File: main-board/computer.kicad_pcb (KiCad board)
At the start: 2 copper layers, 104.1 x 67.3 mm, 17 parts, among them J1 Expansion, J2 Expansion, SW1 RESET, U1 W65C02SxP, U2 28C256, U3 AS6C62256, U4 74HC00, U5 DS1813, X1 1MHz

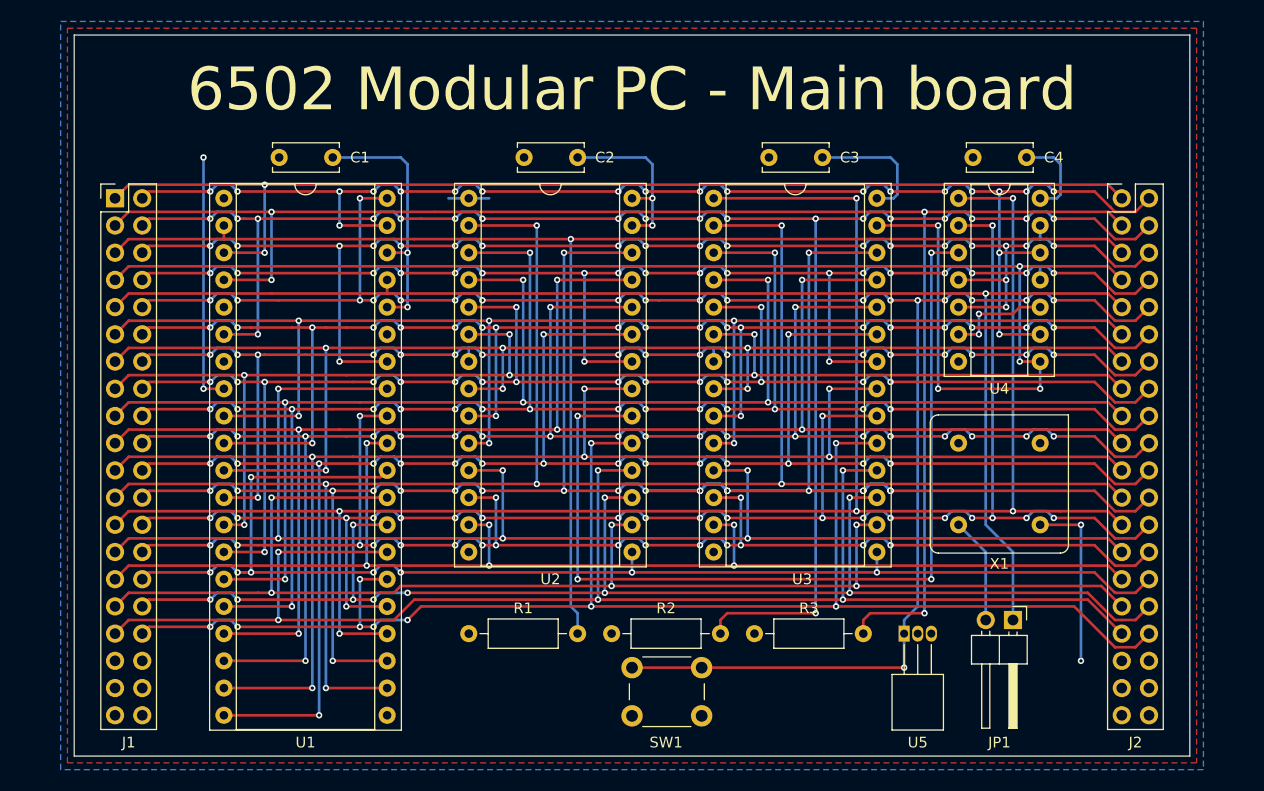
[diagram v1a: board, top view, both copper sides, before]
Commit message: remove vga board, finish other boards
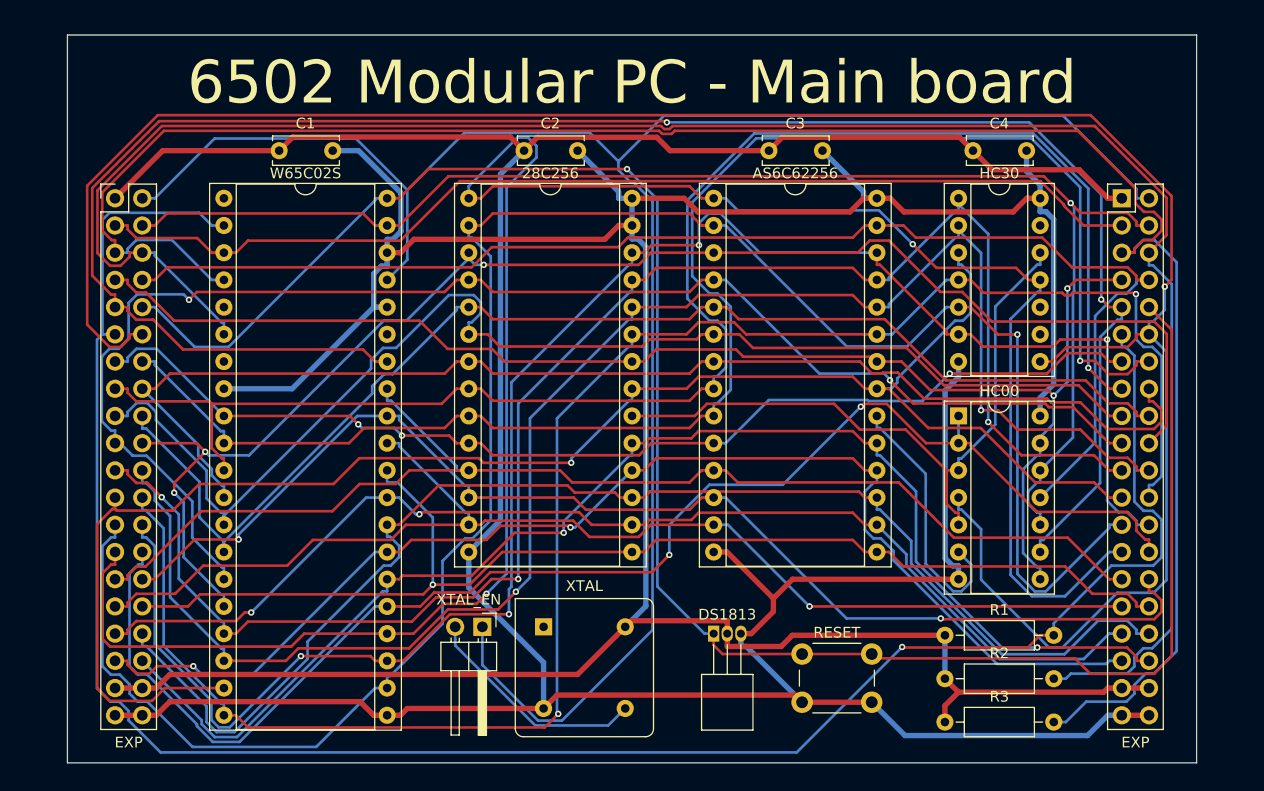
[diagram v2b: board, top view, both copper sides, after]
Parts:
- removed J2: Expansion, Connector_PinHeader_2.54mm:PinHeader_2x20_P2.54mm_Vertical
- removed JP1: Jumper, Connector_PinHeader_2.54mm:PinHeader_1x02_P2.54mm_Horizontal
- removed SW1: RESET, Button_Switch_THT:SW_PUSH_6mm
- removed U1: W65C02SxP, Package_DIP:DIP-40_W15.24mm_Socket
- removed U2: 28C256, Package_DIP:DIP-28_W15.24mm_Socket
- removed U3: AS6C62256, Package_DIP:DIP-28_W15.24mm_Socket
- removed U4: 74HC00, Package_DIP:DIP-14_W7.62mm_Socket
- removed U5: DS1813, Package_TO_SOT_THT:TO-92_Inline_Horizontal1
- removed X1: 1MHz, Oscillator:Oscillator_DIP-8
- added 28C256: 28C256, Package_DIP:DIP-28_W15.24mm_Socket, F.Cu at (104.1, 34.3)
- added AS6C62256: AS6C62256, Package_DIP:DIP-28_W15.24mm_Socket, F.Cu at (127.0, 34.3)
- added DS1813: DS1813, Package_TO_SOT_THT:TO-92_Inline_Horizontal1, F.Cu at (127.0, 74.9)
- added EXP: Expansion, Connector_PinHeader_2.54mm:PinHeader_2x20_P2.54mm_Vertical, F.Cu at (165.1, 34.3)
- added HC00: 74HC00, Package_DIP:DIP-14_W7.62mm_Socket, F.Cu at (149.9, 54.6)
- added HC30: 74HC30, Package_DIP:DIP-14_W7.62mm_Socket, F.Cu at (149.9, 34.3)
- added RESET: RESET, Button_Switch_THT:SW_PUSH_6mm, F.Cu at (135.3, 76.8)
- added W65C02S: W65C02SxP, Package_DIP:DIP-40_W15.24mm_Socket, F.Cu at (81.3, 34.3)
- added XTAL: 1MHz, Oscillator:Oscillator_DIP-8, F.Cu at (111.1, 74.3)
- added XTAL_EN: Jumper, Connector_PinHeader_2.54mm:PinHeader_1x02_P2.54mm_Horizontal, F.Cu at (105.4, 74.3)
- moved R1 44.5 mm to (148.6, 75.1)
- moved R2 31.4 mm to (148.6, 79.1)
- moved R3 19.6 mm to (148.6, 83.2)
- moved C1 0.64 mm to (91.4, 29.8)
- moved C2 0.64 mm to (114.3, 29.8)
- moved C3 0.64 mm to (137.2, 29.8)
- moved C4 0.64 mm to (156.2, 29.8)
- renumbered J1 to EXP
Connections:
- EXP pad 1: PHI1 -> GND
- EXP pad 11: A0 -> RDY
- EXP pad 12: A1 -> !P_SELECT
- EXP pad 13: A2 -> A0
- EXP pad 14: A3 -> A1
- EXP pad 15: A4 -> A2
- EXP pad 16: A5 -> A3
- EXP pad 17: A6 -> A4
- EXP pad 18: A7 -> A5
- EXP pad 19: A8 -> A6
- EXP pad 2: PHI2 -> CLK
- EXP pad 20: A9 -> A7
- EXP pad 21: A10 -> A8
- EXP pad 22: A11 -> A9
- EXP pad 23: A12 -> A10
- EXP pad 24: A13 -> A11
- EXP pad 25: A14 -> A12
- EXP pad 26: !RAM_SELECT -> A13
- EXP pad 27: D0 -> A14
- EXP pad 28: D1 -> A15
- EXP pad 29: D2 -> D0
- EXP pad 3: !IRQ -> PHI1
- EXP pad 30: D3 -> D1
- EXP pad 31: D4 -> D2
- EXP pad 32: D5 -> D3
- EXP pad 33: D6 -> D4
- EXP pad 34: D7 -> D5
- EXP pad 35: +5V -> D6
- EXP pad 36: +5V -> D7
- EXP pad 37: GND -> +5V
- EXP pad 38: GND -> +5V
- EXP pad 4: !NMI -> PHI2
- EXP pad 5: RDY -> !IRQ
- EXP pad 6: R!W -> !NMI
- EXP pad 7: !WRITE -> !READ
- EXP pad 8: !READ -> !WRITE
- EXP pad 9: CLK -> R!W
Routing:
- net GND: track 3.81 -> 319.9 mm
- net !P_SELECT: track 0.00 -> 207.0 mm, vias 0 -> 1
- net +5V: track 101.6 -> 295.7 mm, vias 8 -> 0
- net A15: track 0.00 -> 133.9 mm, vias 0 -> 2
- net !RAM_SELECT: track 156.9 -> 24.8 mm, vias 22 -> 0
- net CLK: track 127.8 -> 186.5 mm, vias 1 -> 0
- net RDY: track 133.4 -> 190.9 mm
- net R!W: track 130.9 -> 178.0 mm, vias 21 -> 2
- net !IRQ: track 150.5 -> 188.0 mm, vias 4 -> 0
- net A13: track 200.7 -> 166.0 mm, vias 22 -> 4
- net A0: track 137.6 -> 103.1 mm, vias 6 -> 3
- net A7: track 164.1 -> 137.6 mm, vias 18 -> 3
- net D6: track 143.6 -> 117.3 mm, vias 6 -> 2
- net A5: track 141.3 -> 117.4 mm, vias 18 -> 0
- net !ROM_SELECT: track 86.4 -> 63.0 mm, vias 4 -> 0
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- removed copper zone on F.Cu, net +5V
- removed copper zone on B.Cu, net GND
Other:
- board size 104.1 x 67.3 mm -> 105.4 x 67.9 mm
- net class Wide added: clearance 0.2, trace_width 0.5, via_dia 0.6, via_drill 0.3
- board text added: "JLCJLCJLCJLC"

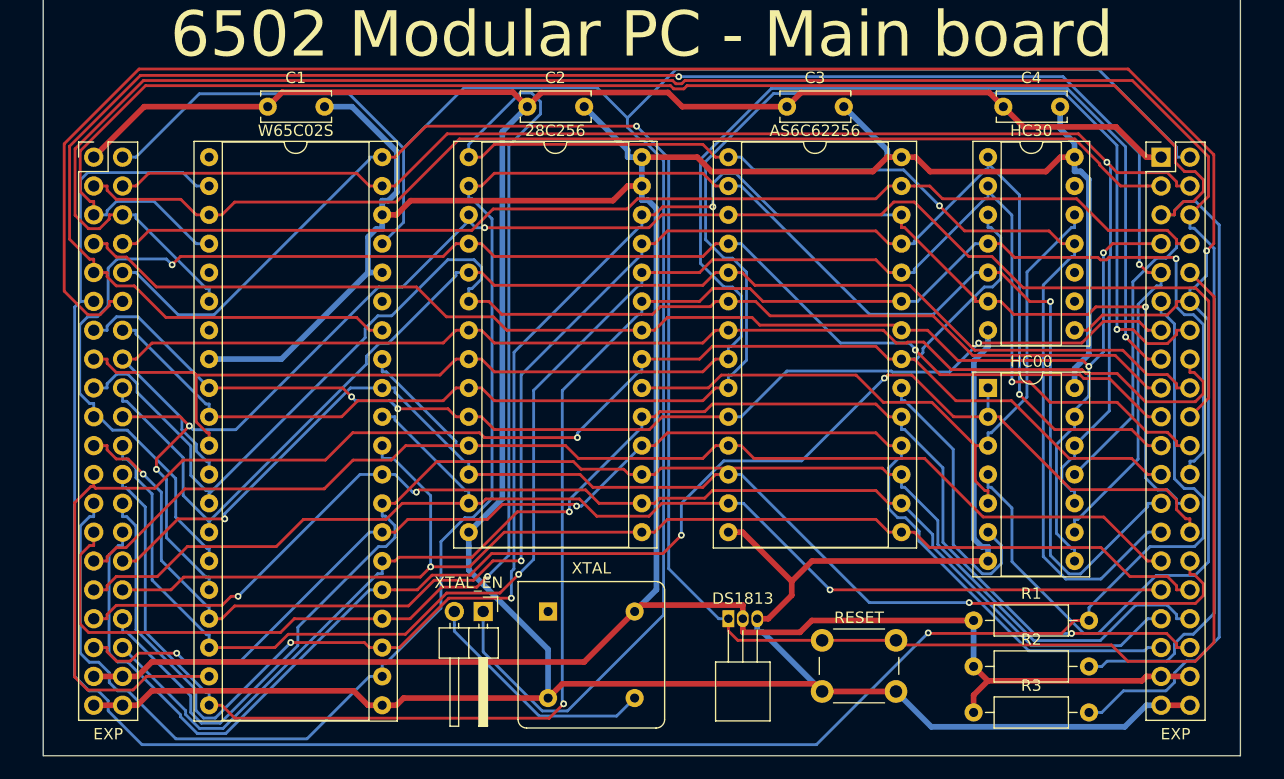
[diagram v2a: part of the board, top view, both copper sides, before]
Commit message: Add VGA socket, fix routing errors on CPU board
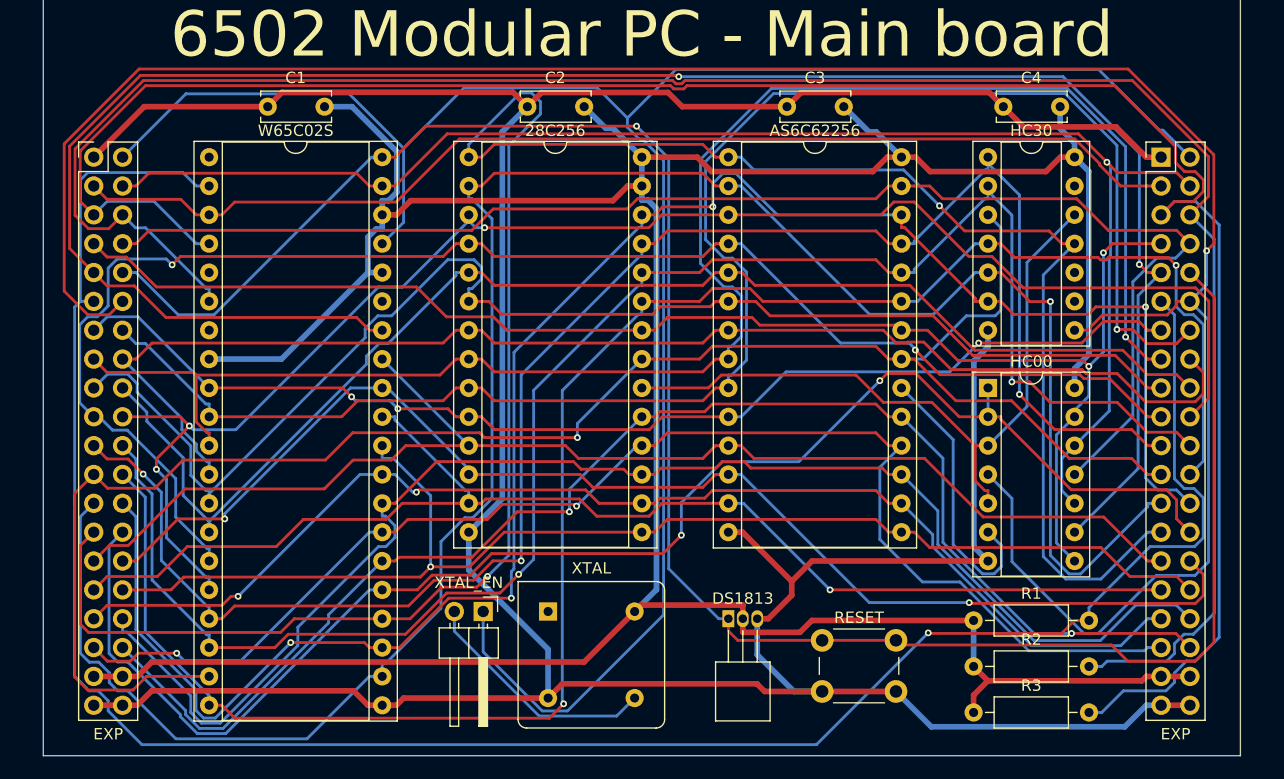
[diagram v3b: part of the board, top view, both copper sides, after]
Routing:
- net D6: track 117.3 -> 119.1 mm
- net A10: track 154.8 -> 156.1 mm
- net D0: track 115.2 -> 114.1 mm
- net +5V: track 295.7 -> 294.7 mm
- net GND: track 319.9 -> 320.7 mm
- net R!W: track 178.0 -> 177.2 mm
- net !IRQ: track 188.0 -> 187.1 mm
- net D1: track 115.5 -> 114.6 mm
- net D7: track 124.5 -> 123.8 mm
- net !NMI: track 183.6 -> 183.0 mm
- net !P_SELECT: track 207.0 -> 206.4 mm
- net A11: track 166.6 -> 166.0 mm
- net PHI2: track 131.7 -> 131.1 mm
- net !READ: track 128.5 -> 127.9 mm
- net CLK: track 186.5 -> 186.0 mm

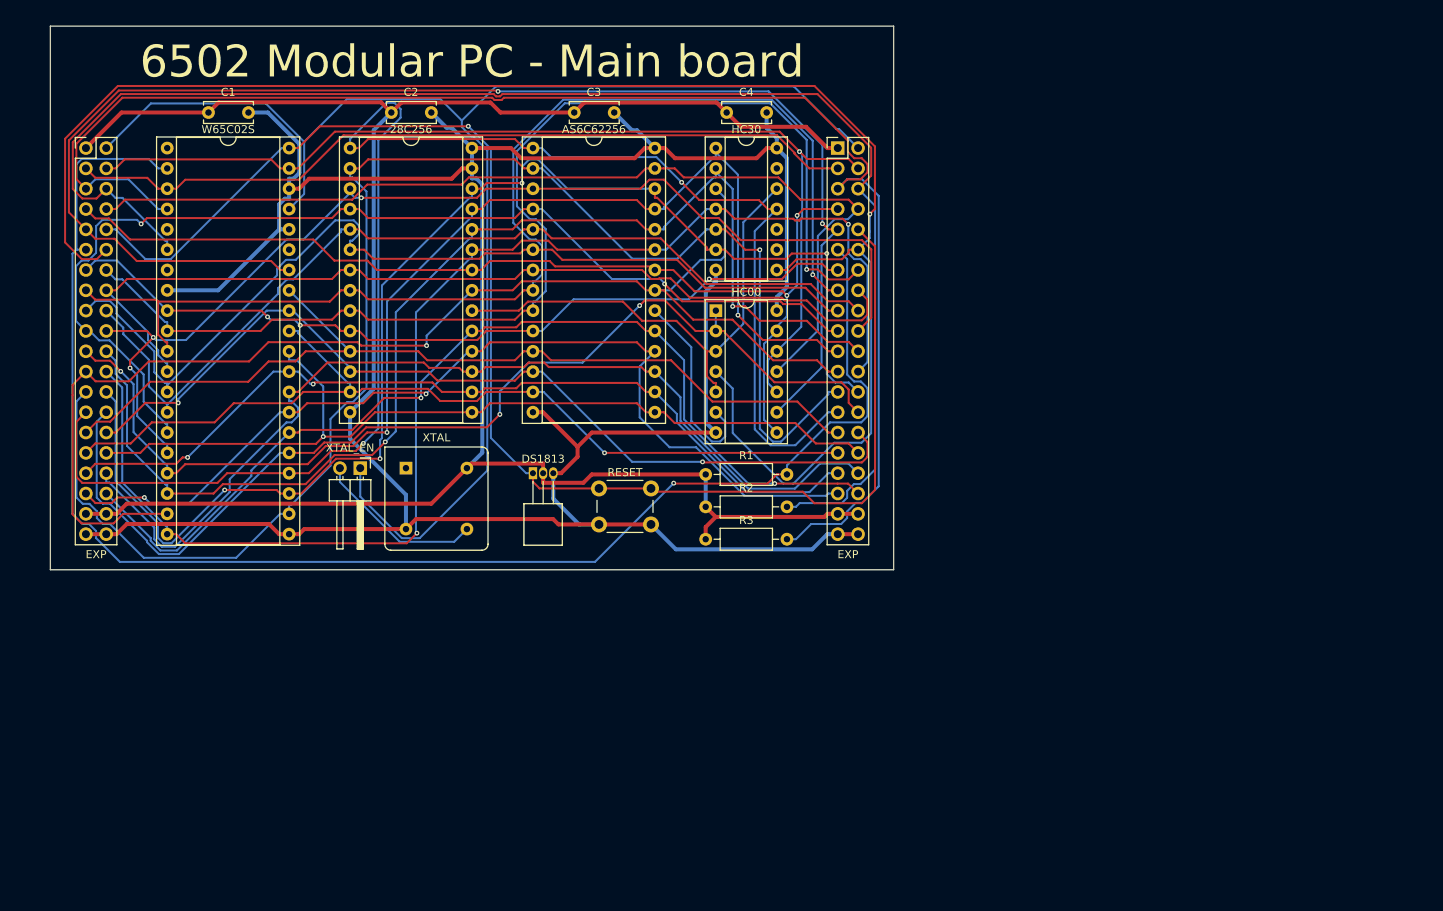
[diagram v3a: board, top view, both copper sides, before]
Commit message: Integtrate IO into mail board, begion VGA layout
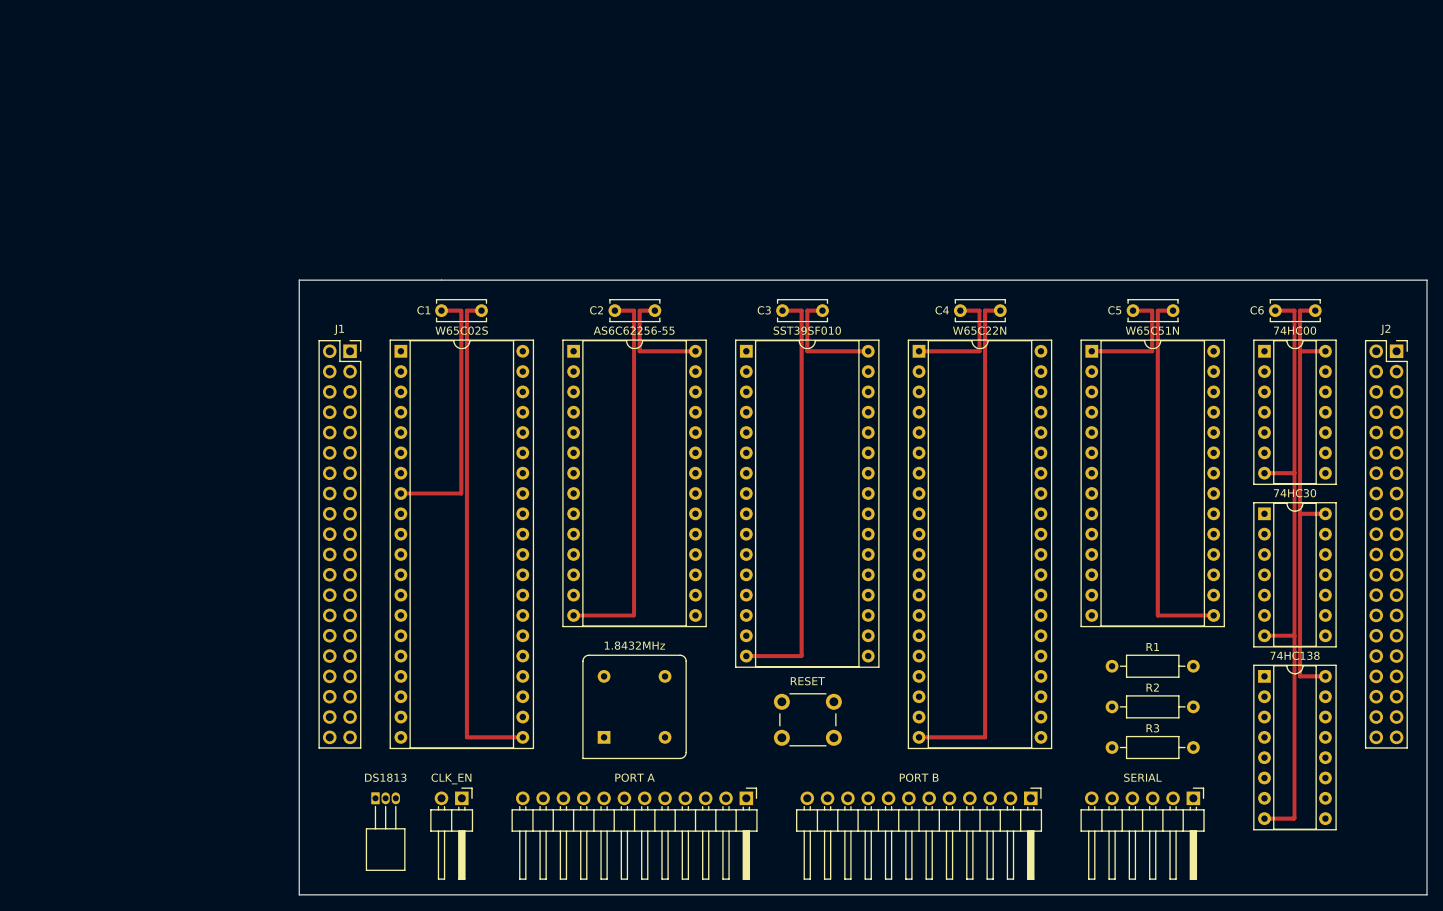
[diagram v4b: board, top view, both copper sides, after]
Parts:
- removed 28C256: 28C256, Package_DIP:DIP-28_W15.24mm_Socket
- removed AS6C62256: AS6C62256, Package_DIP:DIP-28_W15.24mm_Socket
- removed DS1813: DS1813, Package_TO_SOT_THT:TO-92_Inline_Horizontal1
- removed EXP (x2): Expansion, Connector_PinHeader_2.54mm:PinHeader_2x20_P2.54mm_Vertical
- removed HC00: 74HC00, Package_DIP:DIP-14_W7.62mm_Socket
- removed HC30: 74HC30, Package_DIP:DIP-14_W7.62mm_Socket
- removed RESET: RESET, Button_Switch_THT:SW_PUSH_6mm
- removed W65C02S: W65C02SxP, Package_DIP:DIP-40_W15.24mm_Socket
- removed XTAL: 1MHz, Oscillator:Oscillator_DIP-8
- removed XTAL_EN: Jumper, Connector_PinHeader_2.54mm:PinHeader_1x02_P2.54mm_Horizontal
- added C5: 0.1uF, Capacitor_THT:C_Disc_D6.0mm_W2.5mm_P5.00mm, F.Cu at (207.0, 54.6)
- added C6: 0.1uF, Capacitor_THT:C_Disc_D6.0mm_W2.5mm_P5.00mm, F.Cu at (224.8, 54.6)
- added J1: Conn_02x20_Odd_Even, Connector_PinSocket_2.54mm:PinSocket_2x20_P2.54mm_Vertical, F.Cu at (104.1, 59.7)
- added J2: Conn_02x20_Odd_Even, Connector_PinSocket_2.54mm:PinSocket_2x20_P2.54mm_Vertical, F.Cu at (234.9, 59.7)
- added J3: PORT A, Connector_PinHeader_2.54mm:PinHeader_1x12_P2.54mm_Horizontal, F.Cu at (153.7, 115.6)
- added J4: PORT B, Connector_PinHeader_2.54mm:PinHeader_1x12_P2.54mm_Horizontal, F.Cu at (189.2, 115.6)
- added J5: SERIAL, Connector_PinHeader_2.54mm:PinHeader_1x06_P2.54mm_Horizontal, F.Cu at (209.6, 115.6)
- added JP1: CLK_EN, Connector_PinHeader_2.54mm:PinHeader_1x02_P2.54mm_Horizontal, F.Cu at (118.1, 115.6)
- added SW1: RESET, Button_Switch_THT:SW_PUSH_6mm, F.Cu at (158.1, 103.5)
- added U1: W65C02S, Package_DIP:DIP-40_W15.24mm_Socket, F.Cu at (110.5, 59.7)
- added U11: DS1813, Package_TO_SOT_THT:TO-92_Inline_Horizontal1, F.Cu at (107.3, 115.6)
- added U2: AS6C62256-55, Package_DIP:DIP-28_W15.24mm_Socket, F.Cu at (132.1, 59.7)
- added U3: SST39SF010, Package_DIP:DIP-32_W15.24mm_Socket, F.Cu at (153.7, 59.7)
- added U4: W65C22N, Package_DIP:DIP-40_W15.24mm_Socket, F.Cu at (175.3, 59.7)
- added U5: W65C51N, Package_DIP:DIP-28_W15.24mm_Socket, F.Cu at (196.8, 59.7)
- added U6: 74HC00, Package_DIP:DIP-14_W7.62mm_Socket, F.Cu at (218.4, 59.7)
- added U7: 74HC30, Package_DIP:DIP-14_W7.62mm_Socket, F.Cu at (218.4, 80.0)
- added U8: 74HC138, Package_DIP:DIP-16_W7.62mm_Socket, F.Cu at (218.4, 100.3)
- added X1: 1.8432MHz, Oscillator:Oscillator_DIP-8, F.Cu at (135.9, 108.0)
- moved R3 57.1 mm to (199.4, 109.2)
- moved R2 56.6 mm to (199.4, 104.1)
- moved R1 56.2 mm to (199.4, 99.1)
- moved C4 38.3 mm to (185.4, 54.6)
- moved C2 37.3 mm to (142.2, 54.6)
- moved C3 35.9 mm to (163.2, 54.6)
- moved C1 34.6 mm to (115.6, 54.6), turned to 0 degrees
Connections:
- R1 pad 2: RDY -> !IRQ
- R3 pad 2: !IRQ -> RDY
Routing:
- net !P_SELECT: track 206.4 -> 0.00 mm, vias 1 -> 0
- net A14: track 199.2 -> 0.00 mm, vias 2 -> 0
- net RDY: track 190.7 -> 0.00 mm, vias 1 -> 0
- net A12: track 189.9 -> 0.00 mm, vias 1 -> 0
- net !IRQ: track 187.1 -> 0.00 mm
- net CLK: track 186.0 -> 0.00 mm
- net !NMI: track 183.0 -> 0.00 mm
- net !RESET: track 180.0 -> 0.00 mm, vias 1 -> 0
- net R!W: track 177.2 -> 0.00 mm, vias 2 -> 0
- net A11: track 166.0 -> 0.00 mm, vias 2 -> 0
- net A13: track 165.6 -> 0.00 mm, vias 4 -> 0
- net A10: track 156.1 -> 0.00 mm, vias 1 -> 0
- net A8: track 153.9 -> 0.00 mm, vias 3 -> 0
- net A9: track 153.3 -> 0.00 mm, vias 2 -> 0
- net A2: track 147.7 -> 0.00 mm, vias 1 -> 0
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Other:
- board size 105.4 x 67.9 mm -> 141 x 76.8 mm
- board text removed: "6502 Modular PC - Main board"
- board text removed: "JLCJLCJLCJLC"
